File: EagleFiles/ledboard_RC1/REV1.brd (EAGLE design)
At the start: 100 x 100 mm, 164 parts, among them K1 694106105102, Q1_24MHZ ECS-240-18-23A-EN-TR, X1 USBSMD

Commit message: updated board
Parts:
- added C79: 100NF, rcl:C0603
- LDO: value TPS79933 -> TPS73633; device TPS79933:SOT23-DBV -> TPS73633:SOT23-DBV
- moved C70 188.5 mm to (70.6, 49.3), flipped to the bottom
- moved PUSHPULL 179.9 mm to (85.2, 64.4), flipped to the bottom, turned to 270 degrees
- moved C69 179.0 mm to (65.3, 49.2), flipped to the bottom, turned to 180 degrees
- moved R5 172.7 mm to (66.8, 44.8), flipped to the bottom, turned to 90 degrees
- moved R10 172.4 mm to (73.2, 80.3), flipped to the bottom
- moved R4 170.5 mm to (69.4, 44.8), flipped to the bottom, turned to 90 degrees
- moved X1 162.8 mm to (67.5, 26.9), flipped to the bottom, turned to 90 degrees
- moved C78 161.0 mm to (78.5, 76.7), flipped to the bottom, turned to 90 degrees
- moved L1 160.2 mm to (68.1, 34.5), flipped to the bottom, turned to 270 degrees
- moved C68 160.2 mm to (73.7, 40.8), flipped to the bottom
- moved C77 158.3 mm to (78.4, 57.5), flipped to the bottom, turned to 180 degrees
- moved C66 157.6 mm to (43.5, 55.4), flipped to the bottom
- moved C75 157.0 mm to (71.8, 77.0), flipped to the bottom, turned to 90 degrees
- moved FERRITBEAD 154.7 mm to (47.9, 55.3), flipped to the bottom, turned to 180 degrees
- moved LDO 153.2 mm to (39.0, 52.5), flipped to the bottom
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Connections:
- net +5V: now also C79.1
- net GND: now also C79.2
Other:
- outline, holes or cut-outs redrawn
- board text added: "Kond."
- board text added: "Lananschluss"

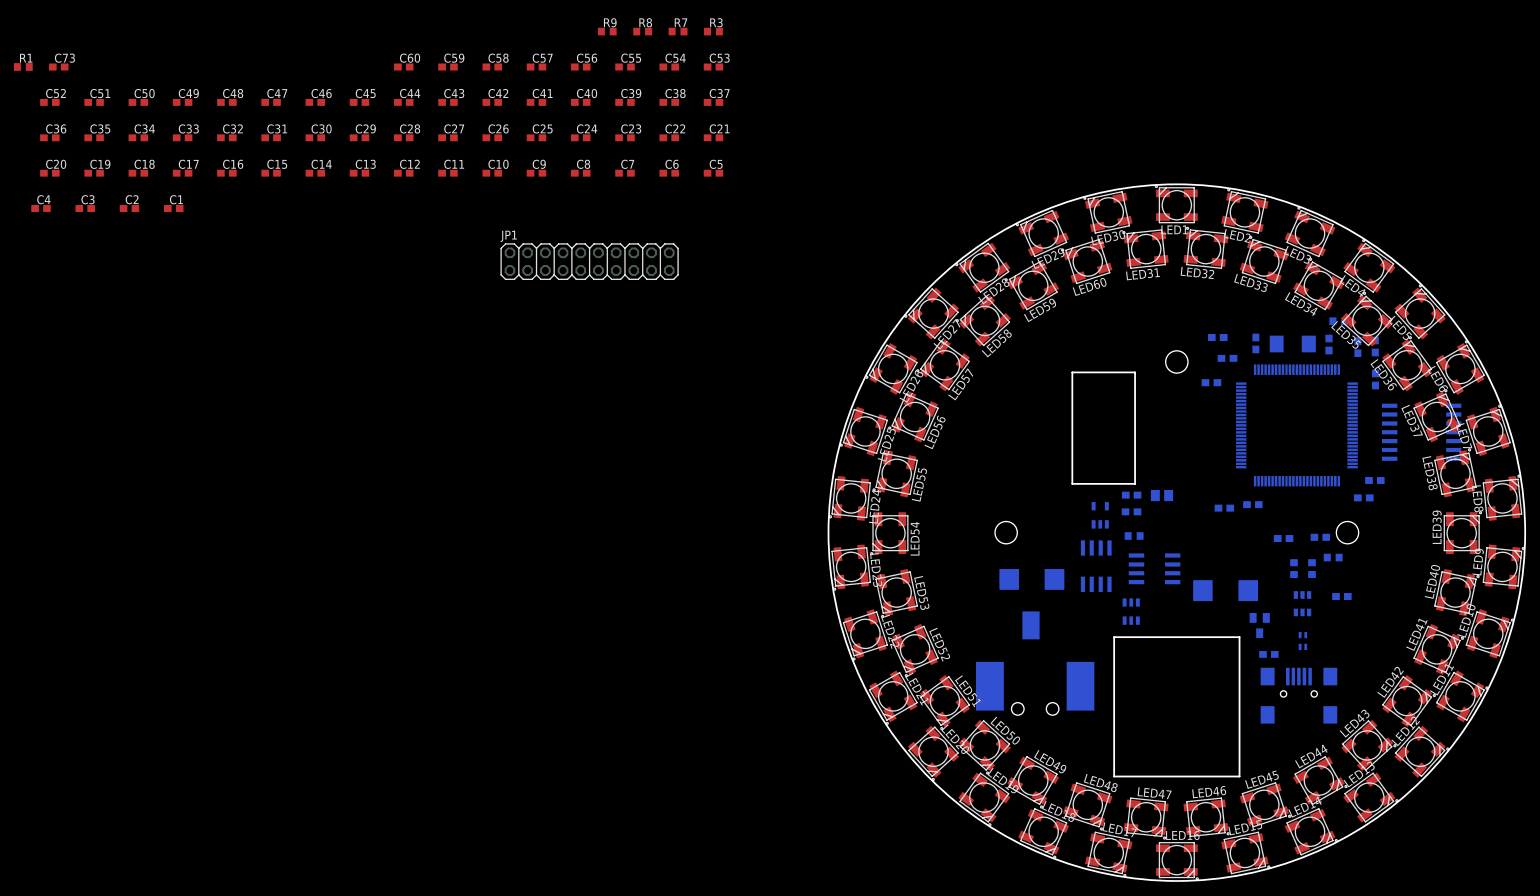
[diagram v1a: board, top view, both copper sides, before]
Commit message: First layout done, few changes for easier routing
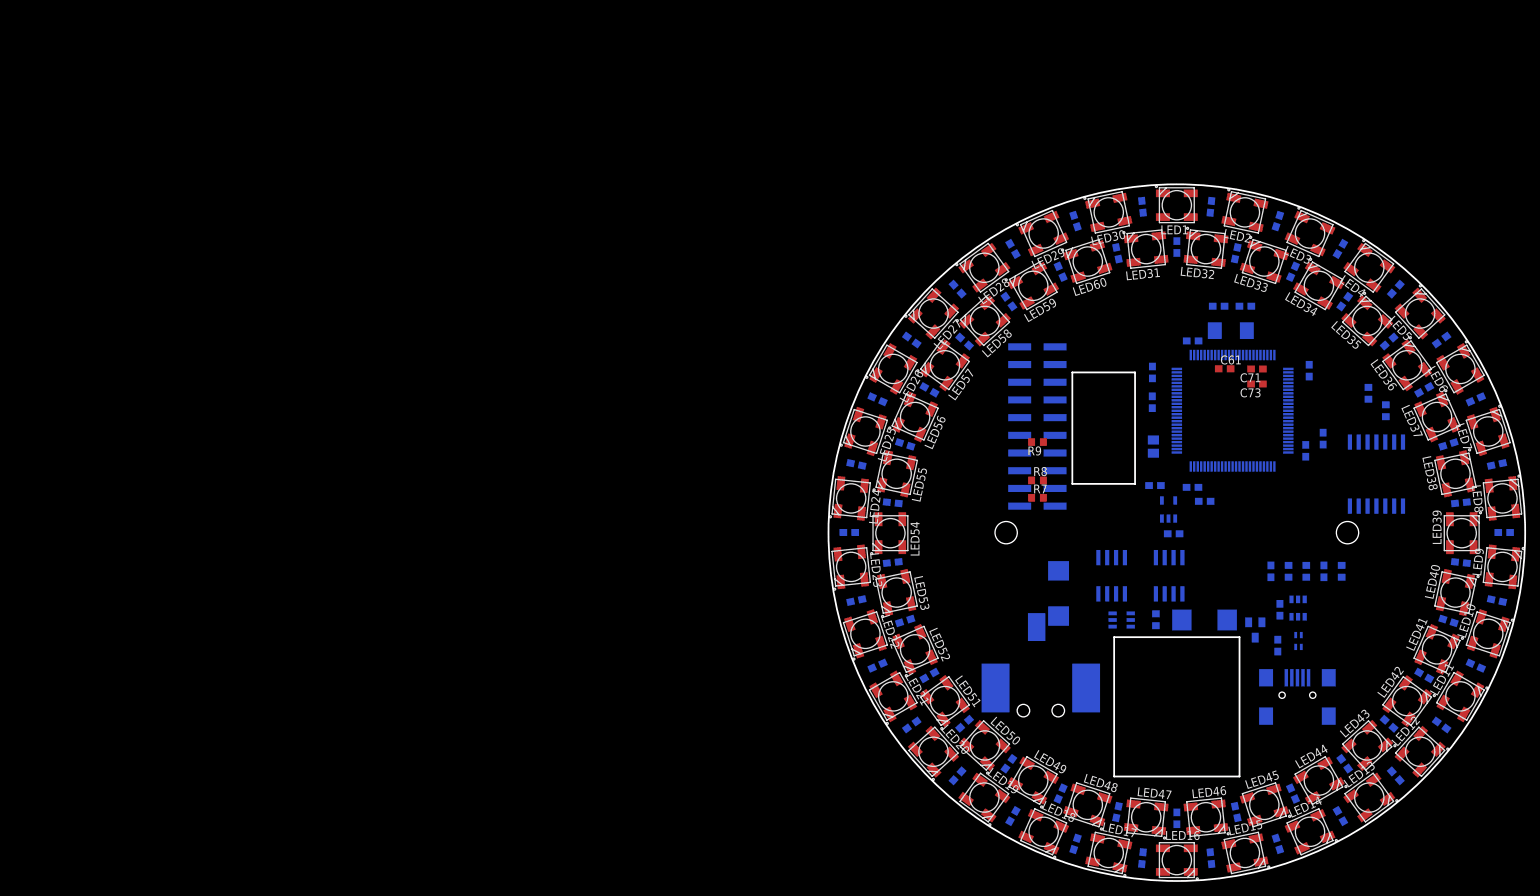
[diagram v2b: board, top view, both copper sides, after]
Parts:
- removed R10: 47, rcl:R0603
- removed SI4465DY_1, SI4465DY_2: (no value), ownLib:SO08
- added T1, T2: SI4465DY, ownLib:SO08
- C67: value 4.7mu -> 4.7µF
- C79: value 100NF -> 100nF
- JP1: device pinhead:2X10 -> pinhead:2X10SMD
- moved C36 200.6 mm to (85.5, 70.5), flipped to the bottom, turned to 150 degrees
- moved R1 198.7 mm to (77.5, 70.0), flipped to the bottom, turned to 90 degrees
- moved C35 188.2 mm to (80.5, 77.4), flipped to the bottom, turned to 138 degrees
- moved C4 186.6 mm to (73.5, 90.7), flipped to the bottom, turned to 120 degrees
- moved C73 177.9 mm to (61.5, 71.3), turned to 180 degrees
- moved C34 174.7 mm to (74.1, 83.2), flipped to the bottom, turned to 126 degrees
- moved C14 173.7 mm to (73.5, 9.32), flipped to the bottom, turned to 240 degrees
- moved C15 173.6 mm to (64.5, 5.33), flipped to the bottom, turned to 252 degrees
- moved C16 172.1 mm to (54.9, 3.28), flipped to the bottom, turned to 264 degrees
- moved C13 172.1 mm to (81.4, 15.1), flipped to the bottom, turned to 228 degrees
- moved C3 171.2 mm to (64.5, 94.7), flipped to the bottom, turned to 108 degrees
- moved C17 169.3 mm to (45.1, 3.28), flipped to the bottom, turned to 276 degrees
- moved C12 168.7 mm to (88.0, 22.4), flipped to the bottom, turned to 216 degrees
- moved C18 165.4 mm to (35.5, 5.33), flipped to the bottom, turned to 288 degrees
- moved C11 163.6 mm to (92.9, 30.9), flipped to the bottom, turned to 204 degrees
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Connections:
- net N$47 renamed D+_TMP
- net N$64 renamed D-_TMP
- removed net N$52: LED35.DOUT, LED36.DIN
- removed net VREF+: MCU.20, R10.2
- new net N$47: LED36.DIN, R1.2
- net +3V3: now also MCU.20; no longer R10.1
- net +5V: now also T1.1, T1.2, T1.3, T2.1, T2.2, T2.3; no longer SI4465DY_1.1, SI4465DY_1.2, SI4465DY_1.3, SI4465DY_2.1, SI4465DY_2.2, SI4465DY_2.3
- net D+: now also C69.2, R5.2; no longer C70.2, R4.2, R6.1
- net D-: now also C70.2, R4.2, R6.1; no longer C69.2, R5.2
- net DATA_IN_1_HIGH: now also R3.1; no longer R1.1
- net DATA_IN_2_HIGH: now also R1.1; no longer R3.1
- net N$1: now also LED45.DOUT; no longer R1.2
- net N$22: now also R3.2; no longer LED5.DOUT
- net N$32: now also LED15.DOUT; no longer R3.2
- net N$63: now also T2.4; no longer SI4465DY_2.4
- net N$65: now also L1.2; no longer L1.3
- net N$66: now also L1.3; no longer L1.2
- net N$70: now also T1.5, T1.6, T1.7, T1.8; no longer SI4465DY_1.5, SI4465DY_1.6, SI4465DY_1.7, SI4465DY_1.8
- net PM_STATUS: now also T1.4; no longer SI4465DY_1.4
- net V_5: now also T2.5, T2.6, T2.7, T2.8; no longer SI4465DY_2.5, SI4465DY_2.6, SI4465DY_2.7, SI4465DY_2.8

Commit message: update
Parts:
- removed FERRITBEAD: MLS0805-4S7-102, MLS0805:M0805
- added C80: 100nF, rcl:C0603
- moved R6 12.5 mm to (61.2, 44.5)
- moved R1 11.1 mm to (84.0, 61.0), flipped to the top, turned to 0 degrees
- moved T2 8.63 mm to (32.1, 45.3), turned to 270 degrees
- moved 4 8.00 mm to (25.0, 41.3)
- moved C62 6.50 mm to (75.0, 70.8)
- moved C63 6.50 mm to (74.5, 59.2)
- moved C64 6.50 mm to (58.2, 54.0)
- moved C65 6.50 mm to (52.5, 70.5)
- moved C74 6.50 mm to (62.0, 80.0)
- moved C76 6.50 mm to (60.0, 52.0)
- moved C77 6.50 mm to (77.0, 61.0)
- moved C78 6.50 mm to (52.5, 66.2)
- moved MCU 6.50 mm to (64.0, 65.0)
- moved Q1_24MHZ 6.50 mm to (63.8, 76.5)
- moved PUSHPULL 6.45 mm to (81.8, 52.8)
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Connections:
- removed net N$54: LED37.DOUT, LED38.DIN
- removed net N$62: C66.1, FERRITBEAD.1, LDO.5
- removed net N$70: 0.5.P$2, T1.5, T1.6, T1.7, T1.8
- new net N$52: LED35.DOUT, LED36.DIN
- new net VBUS_S: 0.5.P$2, C68.2, D1.5, T1.5, T1.6, T1.7, T1.8
- net +3V3: now also C66.1, LDO.5; no longer FERRITBEAD.2
- net D+: now also R6.1
- net D-: no longer R6.1
- net DATA_IN_1_HIGH: now also R1.1; no longer R3.1
- net DATA_IN_2_HIGH: now also R3.1; no longer R1.1
- net GND: now also C80.2
- net N$22: now also LED7.DIN; no longer LED6.DIN
- net N$23: now also LED5.DOUT, LED6.DIN; no longer LED6.DOUT, LED7.DIN
- net N$47: now also LED38.DIN; no longer LED36.DIN
- net VBUS: no longer C68.2, D1.5
- net V_5: now also C80.1
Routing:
- net +3V3: track 0.00 -> 160.0 mm, vias 0 -> 6
- net GND: track 0.00 -> 138.1 mm, vias 0 -> 13
- net PM_STATUS: track 0.00 -> 62.4 mm, vias 0 -> 2
- net NRSTIN: track 0.00 -> 57.3 mm
- net JTDO: track 0.00 -> 53.6 mm
- net JTCK: track 0.00 -> 42.5 mm
- net JTMS: track 0.00 -> 39.5 mm
- net NJTRST: track 0.00 -> 39.0 mm
- net JTDI: track 0.00 -> 35.5 mm
- net +5V: track 0.00 -> 29.8 mm
- net V_5: track 0.00 -> 27.8 mm
- net VBUS_S: track 0.00 -> 26.1 mm
- net D+: track 0.00 -> 19.1 mm
- net N$63: track 0.00 -> 17.7 mm
- net D-: track 0.00 -> 17.6 mm
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- added copper zone on layer 16, net +5V
